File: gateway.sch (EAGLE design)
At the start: 22 parts, among them J1 RASPBERRYPI-40-PIN-GPIO_PTH_N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, Q1 BSS123

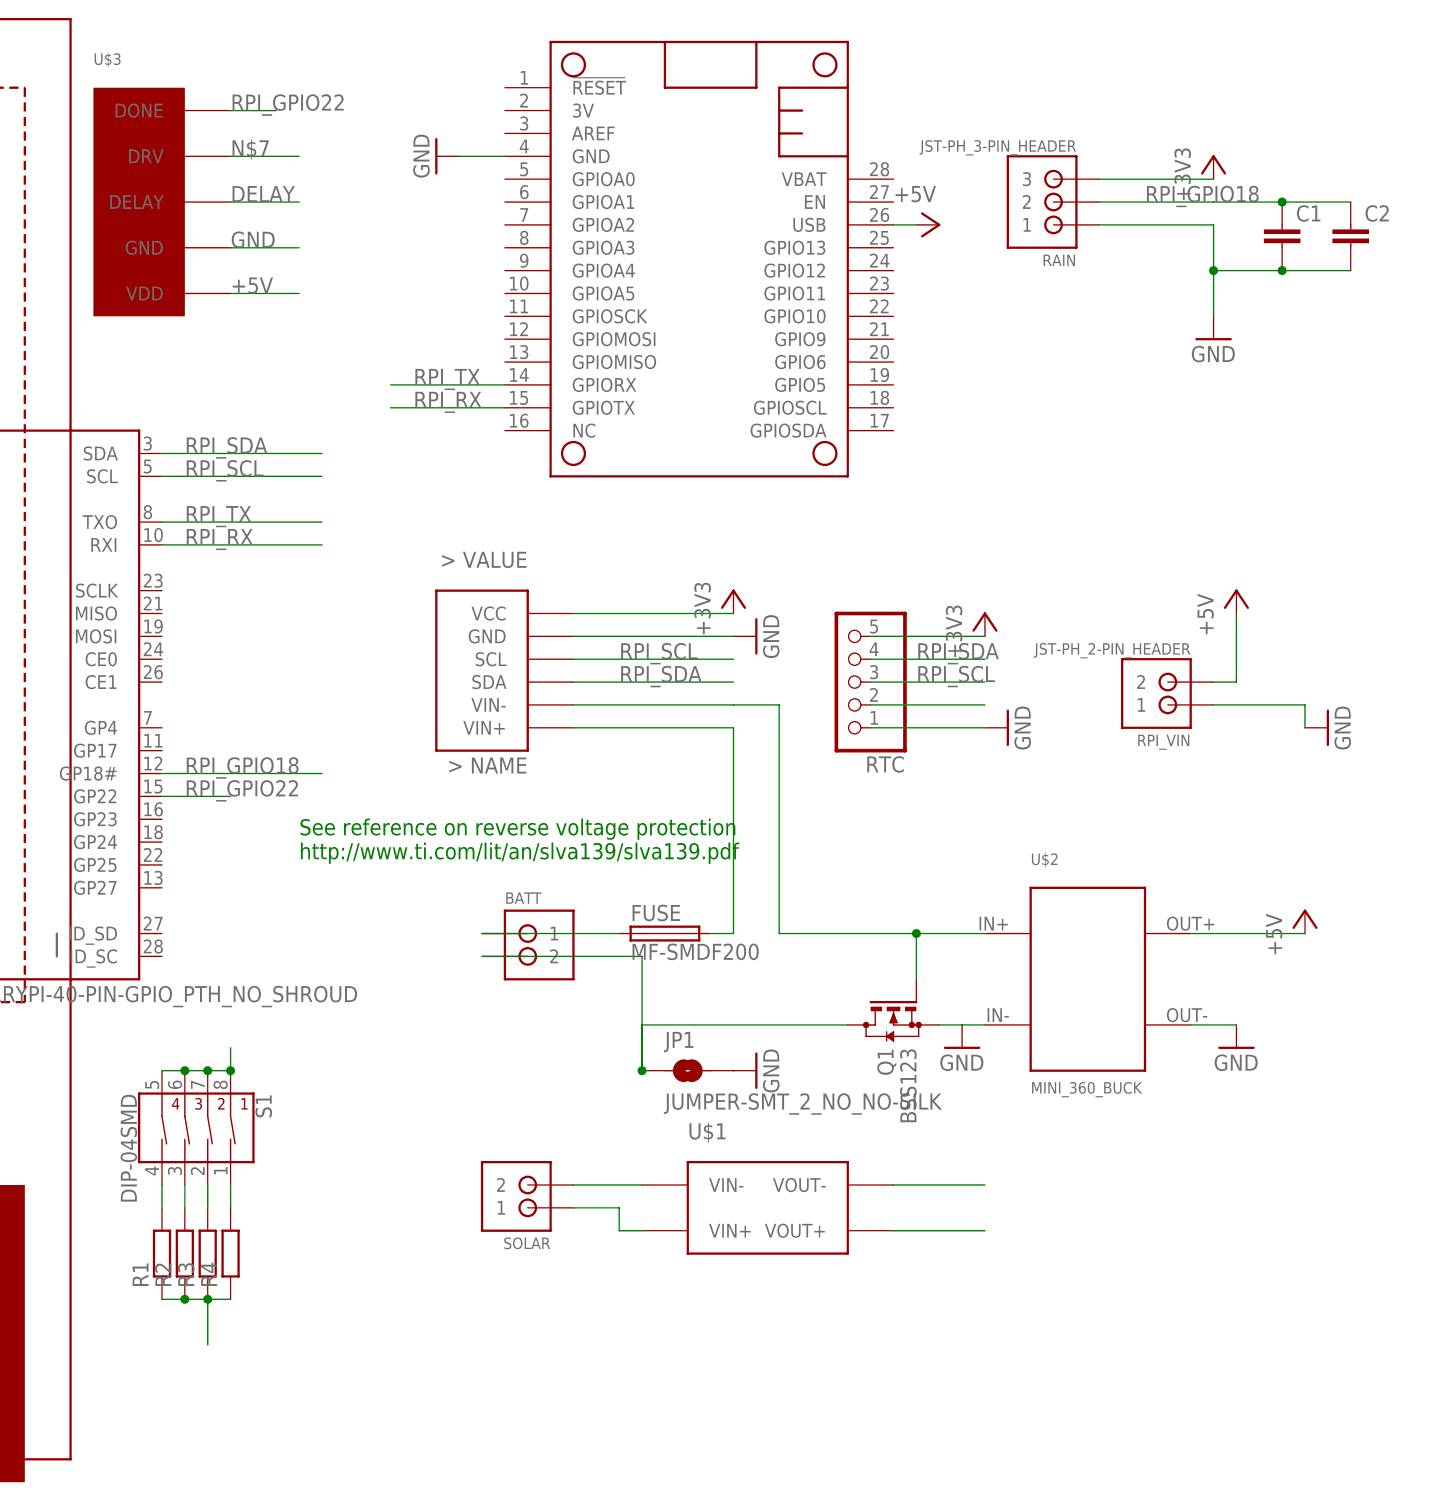
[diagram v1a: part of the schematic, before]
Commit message: added another rtc for feather ( tilt only config )
added the bno05_breakout footprint
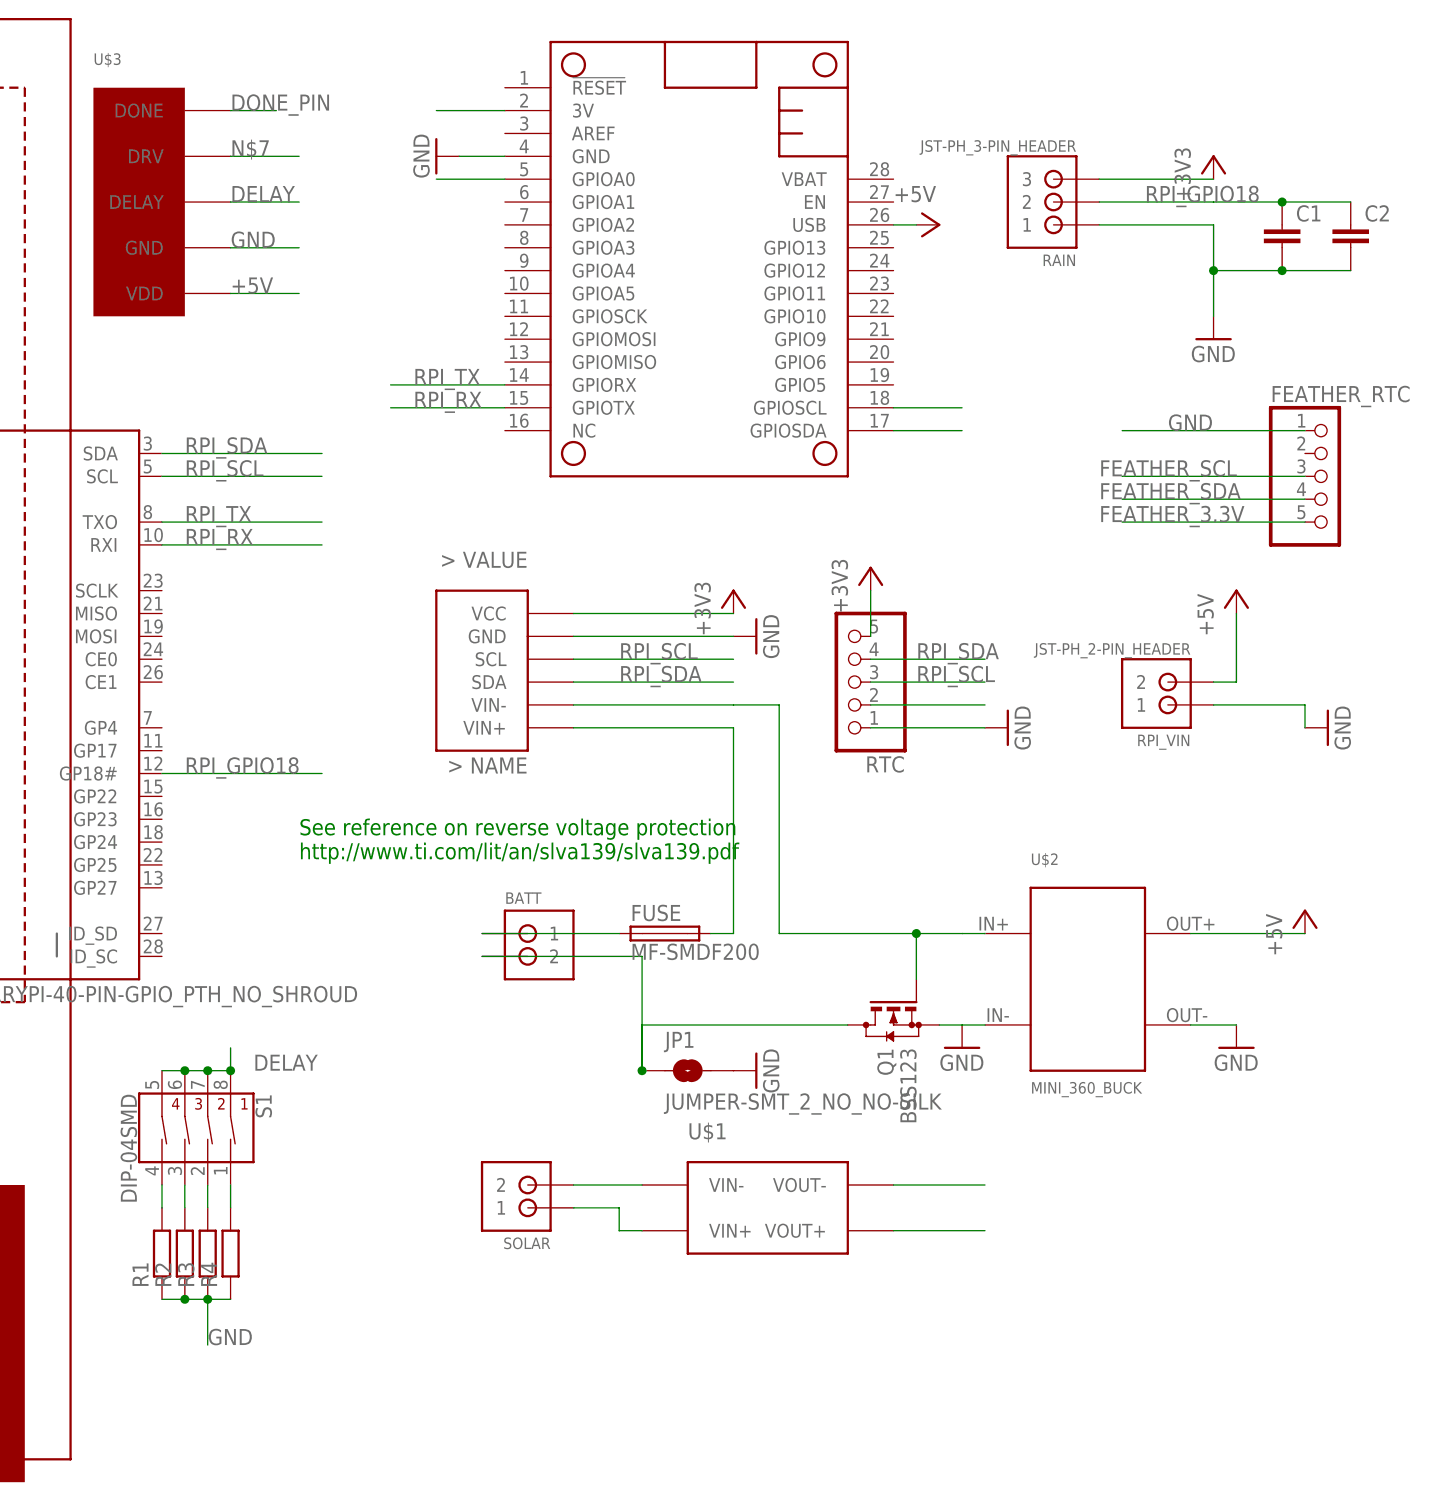
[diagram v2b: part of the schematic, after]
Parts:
- added FEATHER_RTC: (no value), pinhead:PINHD-1X5
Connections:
- removed net N$1: RTC.5
- removed net RPI_GPIO22: J1.GP22, U$3.DONE
- new net DONE_PIN: MS1.GPIOA0, U$3.DONE
- new net FEATHER_3.3V: FEATHER_RTC.5, MS1.3V
- new net FEATHER_SCL: FEATHER_RTC.3, MS1.GPIOSCL
- new net FEATHER_SDA: FEATHER_RTC.4, MS1.GPIOSDA
- net +3V3: now also RTC.5
- net GND: now also FEATHER_RTC.1
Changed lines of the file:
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@@
 <part name="R3" library="rcl" deviceset="R-EU_" device="0204/5"/>
 <part name="R4" library="rcl" deviceset="R-EU_" device="0204/5"/>
+<part name="FEATHER_RTC" library="pinhead" deviceset="PINHD-1X5" device=""/>
 </parts>
 <sheets>
@@
 <instance part="+3V2" gate="G$1" x="81.28" y="121.92"/>
 <instance part="RTC" gate="A" x="193.04" y="96.52" rot="R180"/>
-<instance part="+3V3" gate="G$1" x="208.28" y="104.14"/>
+<instance part="+3V3" gate="G$1" x="195.58" y="109.22"/>
 <instance part="GND4" gate="1" x="210.82" y="91.44" rot="R90"/>
 <instance part="GND5" gate="1" x="76.2" y="101.6" rot="R270"/>
@@
 <instance part="R3" gate="G$1" x="121.92" y="33.02" rot="R90"/>
 <instance part="R4" gate="G$1" x="124.46" y="33.02" rot="R90"/>
+<instance part="FEATHER_RTC" gate="A" x="246.38" y="119.38"/>
 </instances>
 <busses>
@@
 <junction x="121.92" y="27.94"/>
 <wire x1="121.92" y1="27.94" x2="121.92" y2="22.86" width="0.1524" layer="91"/>
+<label x="121.92" y="22.86" size="1.778" layer="95"/>
+</segment>
+<segment>
+<pinref part="FEATHER_RTC" gate="A" pin="1"/>
+<wire x1="243.84" y1="124.46" x2="223.52" y2="124.46" width="0.1524" layer="91"/>
+<label x="228.6" y="124.46" size="1.778" layer="95"/>
 </segment>
 </net>
@@
 <pinref part="RAIN" gate="G$1" pin="3"/>
 </segment>
+<segment>
+<pinref part="RTC" gate="A" pin="5"/>
+<wire x1="195.58" y1="101.6" x2="195.58" y2="106.68" width="0.1524" layer="91"/>
+<pinref part="+3V3" gate="G$1" pin="+3V3"/>
+</segment>
 </net>
 <net name="RPI_SDA" class="0">
@@
 <wire x1="195.58" y1="96.52" x2="208.28" y2="96.52" width="0.1524" layer="91"/>
 <label x="200.66" y="96.52" size="1.778" layer="95"/>
-</segment>
-</net>
-<net name="N$1" class="0">
-<segment>
-<pinref part="RTC" gate="A" pin="5"/>
-<wire x1="195.58" y1="101.6" x2="208.28" y2="101.6" width="0.1524" layer="91"/>
-<pinref part="+3V3" gate="G$1" pin="+3V3"/>
 </segment>
 </net>
@@
 <wire x1="124.46" y1="53.34" x2="124.46" y2="55.88" width="0.1524" layer="91"/>
 <junction x="124.46" y="53.34"/>
+<label x="127" y="53.34" size="1.778" layer="95"/>
 </segment>
 </net>
@@
 </segment>
 </net>
-<net name="RPI_GPIO22" class="0">
-<segment>
-<pinref part="J1" gate="G$1" pin="GP22"/>
-<wire x1="116.84" y1="83.82" x2="124.46" y2="83.82" width="0.1524" layer="91"/>
-<label x="119.38" y="83.82" size="1.778" layer="95"/>
-</segment>
+<net name="DONE_PIN" class="0">
 <segment>
 <pinref part="U$3" gate="G$1" pin="DONE"/>
@@
 <label x="124.46" y="160.02" size="1.778" layer="95"/>
 </segment>
-</net>
+<segment>
+<pinref part="MS1" gate="G$1" pin="GPIOA0"/>
+<wire x1="154.94" y1="152.4" x2="147.32" y2="152.4" width="0.1524" layer="91"/>
+</segment>
+</net>
+<net name="FEATHER_SCL" class="0">
+<segment>
+<pinref part="MS1" gate="G$1" pin="GPIOSCL"/>
+<wire x1="198.12" y1="127" x2="205.74" y2="127" width="0.1524" layer="91"/>
+</segment>
+<segment>
+<pinref part="FEATHER_RTC" gate="A" pin="3"/>
+<wire x1="243.84" y1="119.38" x2="223.52" y2="119.38" width="0.1524" layer="91"/>
+<label x="220.98" y="119.38" size="1.778" layer="95"/>
+</segment>
+</net>
+<net name="FEATHER_SDA" class="0">
+<segment>
+<pinref part="MS1" gate="G$1" pin="GPIOSDA"/>
+<wire x1="198.12" y1="124.46" x2="205.74" y2="124.46" width="0.1524" layer="91"/>
+</segment>
+<segment>
+<pinref part="FEATHER_RTC" gate="A" pin="4"/>
+<wire x1="243.84" y1="116.84" x2="223.52" y2="116.84" width="0.1524" layer="91"/>
+<label x="220.98" y="116.84" size="1.778" layer="95"/>
+</segment>
+</net>
+<net name="FEATHER_3.3V" class="0">
+<segment>
+<pinref part="MS1" gate="G$1" pin="3V"/>
+<wire x1="154.94" y1="160.02" x2="147.32" y2="160.02" width="0.1524" layer="91"/>
+</segment>
+<segment>
+<pinref part="FEATHER_RTC" gate="A" pin="5"/>
+<wire x1="243.84" y1="114.3" x2="223.52" y2="114.3" width="0.1524" layer="91"/>
+<label x="220.98" y="114.3" size="1.778" layer="95"/>
+</segment>
+</net>

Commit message: finished routing
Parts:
- added TILT_SUPPLY: JUMPER-SMT_2_NO_NO-SILK, SparkFun-Jumpers:JUMPER-SMT_2_NO_NO-SILK
- added U$4: BNO05_BREAKOUT, edc_modules:BNO05_BREAKOUT
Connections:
- net N$5 renamed INA_VIN-
- net N$6 renamed INA_VIN+
- net N$8 renamed SOLAR+
- removed net N$7: U$3.DRV
- removed net USB: MS1.USB
- new net FEATHER_USB: MS1.USB, TILT_SUPPLY.2, U$3.DRV
- new net N$1: MS1.EN
- new net N$2: J1.5V@2
- new net N$3: J1.5V@4
- net +3V3: no longer INA219.VCC, RAIN.3
- net +5V: now also TILT_SUPPLY.1
- net FEATHER_3.3V: now also INA219.VCC, RAIN.3, U$4.3V3
- net FEATHER_SCL: now also U$4.SCL
- net FEATHER_SDA: now also U$4.SDA
- net GND: now also U$4.GND
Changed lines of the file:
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@@
 </classes>
 <parts>
-<part name="FRAME1" library="frames" deviceset="A4L-LOC" device=""/>
+<part name="FRAME1" library="frames" deviceset="FRAME_B_L" device=""/>
 <part name="MS1" library="adafruit" deviceset="FEATHERWING" device="_NODIM"/>
 <part name="GND1" library="supply1" deviceset="GND" device=""/>
@@
 <part name="RPI_VIN" library="SRG" deviceset="JST-PH_2-PIN_HEADER" device=""/>
 <part name="RAIN" library="SRG" deviceset="JST-PH_3-PIN_HEADER" device=""/>
-<part name="P+3" library="supply1" deviceset="+5V" device=""/>
 <part name="GND11" library="supply1" deviceset="GND" device=""/>
 <part name="BATT" library="SRG" deviceset="JST-PH_2-PIN_HEADER" device=""/>
-<part name="INA219" library="edc_modules" deviceset="INA219" device=""/>
+<part name="INA219" library="edc_modules" deviceset="INA219" device="" value=""/>
 <part name="PCB2" library="e14_Rpi3_RevA" deviceset="RPI3_NO_GPIO" device=""/>
 <part name="J1" library="SparkFun-Connectors" deviceset="RASPBERRYPI-40-PIN-GPIO" device="_PTH_NO_SHROUD"/>
@@
 <part name="R4" library="rcl" deviceset="R-EU_" device="0204/5"/>
 <part name="FEATHER_RTC" library="pinhead" deviceset="PINHD-1X5" device=""/>
+<part name="FRAME2" library="frames" deviceset="DINA4_L" device=""/>
+<part name="U$4" library="edc_modules" deviceset="BNO05_BREAKOUT" device=""/>
+<part name="TILT_SUPPLY" library="SparkFun-Jumpers" deviceset="JUMPER-SMT_2_NO" device="_NO-SILK" value=""/>
 </parts>
 <sheets>
@@
 <instance part="GND3" gate="1" x="182.88" y="101.6" rot="R90"/>
 <instance part="+3V1" gate="G$1" x="180.34" y="106.68"/>
-<instance part="+3V2" gate="G$1" x="81.28" y="121.92"/>
+<instance part="+3V2" gate="G$1" x="76.2" y="119.38"/>
 <instance part="RTC" gate="A" x="193.04" y="96.52" rot="R180"/>
 <instance part="+3V3" gate="G$1" x="195.58" y="109.22"/>
@@
 <instance part="U$2" gate="G$1" x="213.36" y="53.34"/>
 <instance part="RPI_VIN" gate="G$1" x="226.06" y="96.52" rot="R180"/>
-<instance part="RAIN" gate="G$1" x="215.9" y="149.86" rot="R180"/>
-<instance part="P+3" gate="1" x="203.2" y="147.32" rot="R270"/>
+<instance part="RAIN" gate="G$1" x="215.9" y="149.86" smashed="yes" rot="R180">
+<attribute name="NAME" x="218.44" y="144.018" size="1.27" layer="95" rot="R180"/>
+</instance>
 <instance part="GND11" gate="1" x="236.22" y="55.88"/>
 <instance part="BATT" gate="G$1" x="160.02" y="66.04" smashed="yes">
 <attribute name="NAME" x="154.94" y="71.882" size="1.27" layer="95" font="vector"/>
 </instance>
-<instance part="INA219" gate="G$1" x="157.48" y="96.52" rot="MR0"/>
+<instance part="INA219" gate="G$1" x="157.48" y="96.52" smashed="yes" rot="MR0"/>
 <instance part="PCB2" gate="G$1" x="5.08" y="170.18" rot="R270"/>
 <instance part="J1" gate="G$1" x="101.6" y="96.52"/>
@@
 <instance part="R4" gate="G$1" x="124.46" y="33.02" rot="R90"/>
 <instance part="FEATHER_RTC" gate="A" x="246.38" y="119.38"/>
+<instance part="FRAME2" gate="G$2" x="325.12" y="0"/>
+<instance part="U$4" gate="G$1" x="281.94" y="149.86"/>
+<instance part="TILT_SUPPLY" gate="G$1" x="203.2" y="177.8" smashed="yes">
+<attribute name="NAME" x="200.66" y="180.34" size="1.778" layer="95" font="vector"/>
+</instance>
 </instances>
 <busses>
@@
 <label x="228.6" y="124.46" size="1.778" layer="95"/>
 </segment>
-</net>
-<net name="N$5" class="0">
+<segment>
+<wire x1="276.86" y1="160.02" x2="266.7" y2="160.02" width="0.1524" layer="91"/>
+<pinref part="U$4" gate="G$1" pin="GND"/>
+<label x="261.62" y="160.02" size="1.778" layer="95"/>
+</segment>
+</net>
+<net name="INA_VIN-" class="0">
 <segment>
 <wire x1="162.56" y1="93.98" x2="180.34" y2="93.98" width="0.1524" layer="91"/>
@@
 <net name="+3V3" class="0">
 <segment>
-<wire x1="162.56" y1="104.14" x2="180.34" y2="104.14" width="0.1524" layer="91"/>
-<pinref part="+3V1" gate="G$1" pin="+3V3"/>
-<pinref part="INA219" gate="G$1" pin="VCC"/>
-</segment>
-<segment>
 <pinref part="+3V2" gate="G$1" pin="+3V3"/>
-<wire x1="86.36" y1="116.84" x2="81.28" y2="116.84" width="0.1524" layer="91"/>
-<wire x1="81.28" y1="116.84" x2="81.28" y2="119.38" width="0.1524" layer="91"/>
+<wire x1="86.36" y1="116.84" x2="76.2" y2="116.84" width="0.1524" layer="91"/>
 <pinref part="J1" gate="G$1" pin="3.3V@1"/>
-</segment>
-<segment>
-<wire x1="220.98" y1="152.4" x2="233.68" y2="152.4" width="0.1524" layer="91"/>
-<pinref part="+3V5" gate="G$1" pin="+3V3"/>
-<pinref part="RAIN" gate="G$1" pin="3"/>
 </segment>
 <segment>
@@
 <label x="124.46" y="139.7" size="1.778" layer="95"/>
 </segment>
-</net>
-<net name="USB" class="0">
-<segment>
-<pinref part="P+3" gate="1" pin="+5V"/>
-<pinref part="MS1" gate="G$1" pin="USB"/>
-<wire x1="200.66" y1="147.32" x2="198.12" y2="147.32" width="0.1524" layer="91"/>
-</segment>
-</net>
-<net name="N$6" class="0">
+<segment>
+<pinref part="TILT_SUPPLY" gate="G$1" pin="1"/>
+<wire x1="198.12" y1="177.8" x2="187.96" y2="177.8" width="0.1524" layer="91"/>
+<label x="182.88" y="177.8" size="1.778" layer="95"/>
+</segment>
+</net>
+<net name="INA_VIN+" class="0">
 <segment>
 <pinref part="FUSE" gate="A" pin="2"/>
@@
 </segment>
 </net>
-<net name="N$8" class="0">
+<net name="SOLAR+" class="0">
 <segment>
 <pinref part="SOLAR" gate="G$1" pin="1"/>
@@
 <pinref part="U$1" gate="G$1" pin="VIN+"/>
 <wire x1="167.64" y1="35.56" x2="170.18" y2="35.56" width="0.1524" layer="91"/>
-</segment>
-</net>
-<net name="N$7" class="0">
-<segment>
-<pinref part="U$3" gate="G$1" pin="DRV"/>
-<wire x1="124.46" y1="154.94" x2="132.08" y2="154.94" width="0.1524" layer="91"/>
-<label x="124.46" y="154.94" size="1.778" layer="95"/>
 </segment>
 </net>
@@
 <pinref part="MS1" gate="G$1" pin="GPIOSCL"/>
 <wire x1="198.12" y1="127" x2="205.74" y2="127" width="0.1524" layer="91"/>
+<label x="200.66" y="127" size="1.778" layer="95"/>
 </segment>
 <segment>
@@
 <label x="220.98" y="119.38" size="1.778" layer="95"/>
 </segment>
+<segment>
+<wire x1="276.86" y1="154.94" x2="266.7" y2="154.94" width="0.1524" layer="91"/>
+<label x="261.62" y="154.94" size="1.778" layer="95"/>
+<pinref part="U$4" gate="G$1" pin="SCL"/>
+</segment>
 </net>
 <net name="FEATHER_SDA" class="0">
@@
 <pinref part="MS1" gate="G$1" pin="GPIOSDA"/>
 <wire x1="198.12" y1="124.46" x2="205.74" y2="124.46" width="0.1524" layer="91"/>
+<label x="200.66" y="124.46" size="1.778" layer="95"/>
 </segment>
 <segment>
@@
 <label x="220.98" y="116.84" size="1.778" layer="95"/>
 </segment>
+<segment>
+<wire x1="276.86" y1="157.48" x2="266.7" y2="157.48" width="0.1524" layer="91"/>
+<label x="261.62" y="157.48" size="1.778" layer="95"/>
+<pinref part="U$4" gate="G$1" pin="SDA"/>
+</segment>
 </net>
 <net name="FEATHER_3.3V" class="0">
@@
 <pinref part="MS1" gate="G$1" pin="3V"/>
 <wire x1="154.94" y1="160.02" x2="147.32" y2="160.02" width="0.1524" layer="91"/>
+<label x="139.7" y="160.02" size="1.778" layer="95"/>
 </segment>
 <segment>
@@
 <label x="220.98" y="114.3" size="1.778" layer="95"/>
 </segment>
-</net>
+<segment>
+<wire x1="276.86" y1="162.56" x2="266.7" y2="162.56" width="0.1524" layer="91"/>
+<pinref part="U$4" gate="G$1" pin="3V3"/>
+<label x="261.62" y="162.56" size="1.778" layer="95"/>
+</segment>
+<segment>
+<wire x1="162.56" y1="104.14" x2="180.34" y2="104.14" width="0.1524" layer="91"/>
+<pinref part="+3V1" gate="G$1" pin="+3V3"/>
+<pinref part="INA219" gate="G$1" pin="VCC"/>
+</segment>
+<segment>
+<wire x1="220.98" y1="152.4" x2="233.68" y2="152.4" width="0.1524" layer="91"/>
+<pinref part="+3V5" gate="G$1" pin="+3V3"/>
+<pinref part="RAIN" gate="G$1" pin="3"/>
+</segment>
+</net>
+<net name="N$1" class="0">
+<segment>
+<pinref part="MS1" gate="G$1" pin="EN"/>
+<wire x1="198.12" y1="149.86" x2="205.74" y2="149.86" width="0.1524" layer="91"/>
+<wire x1="205.74" y1="149.86" x2="205.74" y2="165.1" width="0.1524" layer="91"/>
+</segment>
+</net>
+<net name="FEATHER_USB" class="0">
+<segment>
+<pinref part="TILT_SUPPLY" gate="G$1" pin="2"/>
+<wire x1="208.28" y1="177.8" x2="215.9" y2="177.8" width="0.1524" layer="91"/>
+<label x="208.28" y="177.8" size="1.778" layer="95"/>
+</segment>
+<segment>
+<pinref part="MS1" gate="G$1" pin="USB"/>
+<wire x1="198.12" y1="147.32" x2="205.74" y2="147.32" width="0.1524" layer="91"/>
+<wire x1="205.74" y1="147.32" x2="205.74" y2="142.24" width="0.1524" layer="91"/>
+</segment>
+<segment>
+<pinref part="U$3" gate="G$1" pin="DRV"/>
+<wire x1="124.46" y1="154.94" x2="132.08" y2="154.94" width="0.1524" layer="91"/>
+<label x="124.46" y="154.94" size="1.778" layer="95"/>
+</segment>
+</net>
+<net name="N$2" class="0">
+<segment>
+<pinref part="J1" gate="G$1" pin="5V@2"/>
+<wire x1="86.36" y1="121.92" x2="83.82" y2="121.92" width="0.1524" layer="91"/>
+<wire x1="83.82" y1="121.92" x2="83.82" y2="129.54" width="0.1524" layer="91"/>
+</segment>
+</net>
+<net name="N$3" class="0">
+<segment>
+<pinref part="J1" gate="G$1" pin="5V@4"/>
+<wire x1="86.36" y1="119.38" x2="81.28" y2="119.38" width="0.1524" layer="91"/>
+<wire x1="81.28" y1="119.38" x2="81.28" y2="129.54" width="0.1524" layer="91"/>
+</segment>
+</net>
